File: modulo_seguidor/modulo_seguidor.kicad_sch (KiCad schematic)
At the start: 28 parts, among them J1 Battery, J2 Motor A Entradas, J4 Motor IZQ Arduino OUTPUT, J6 puerto sensores, M1 Motor_IZQ, M2 Motor_DER, SW1 SW_Push, SW2 SW_Nidec_CAS-120A1, U1 LM7806_TO220, U2 L298N

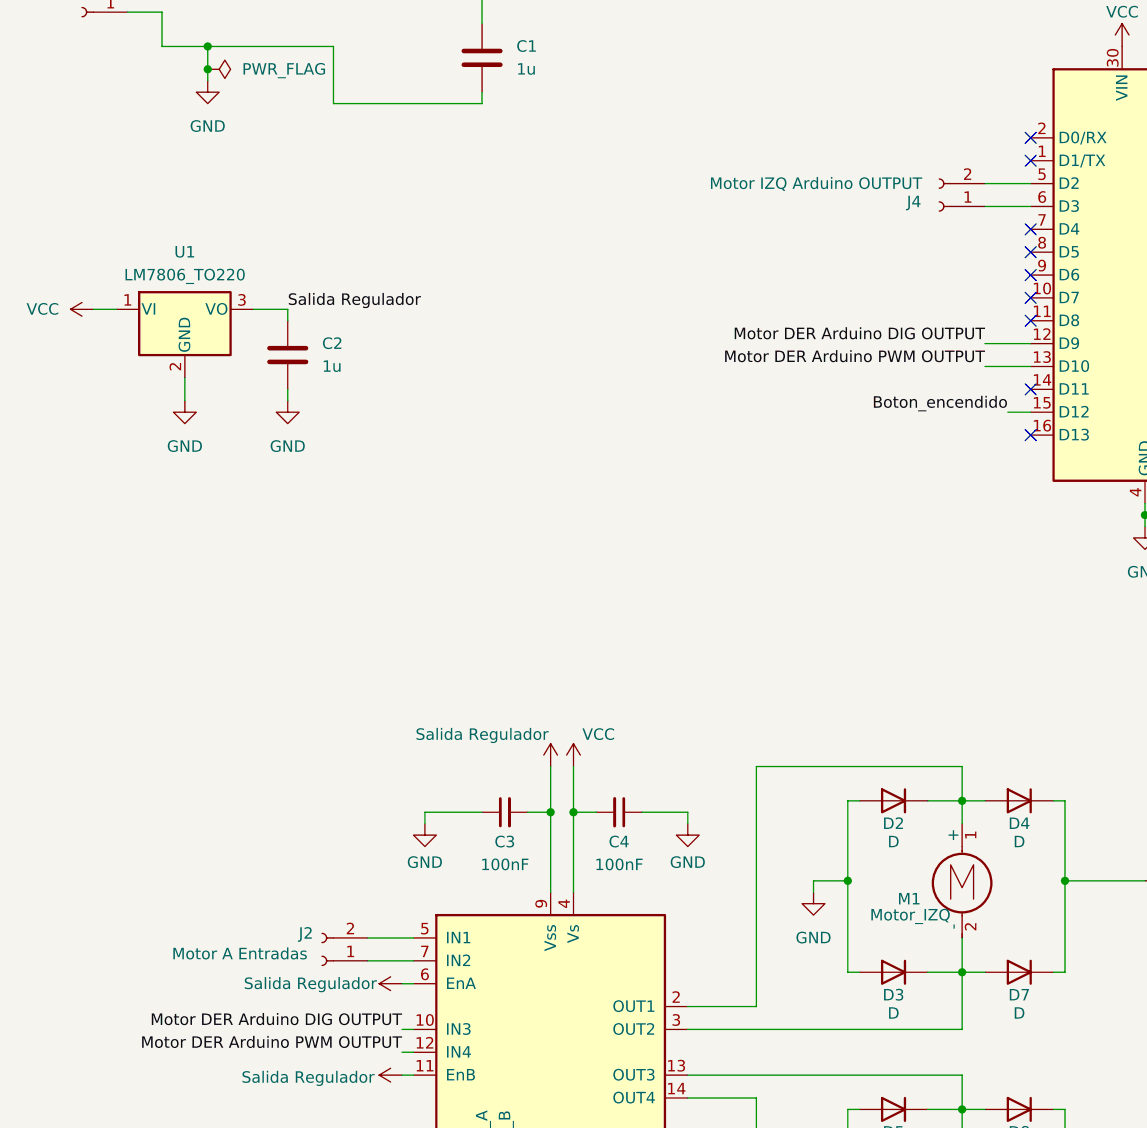
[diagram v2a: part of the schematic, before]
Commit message: refactor(modulo-seguidor): Elimino jumpers por cables soldados
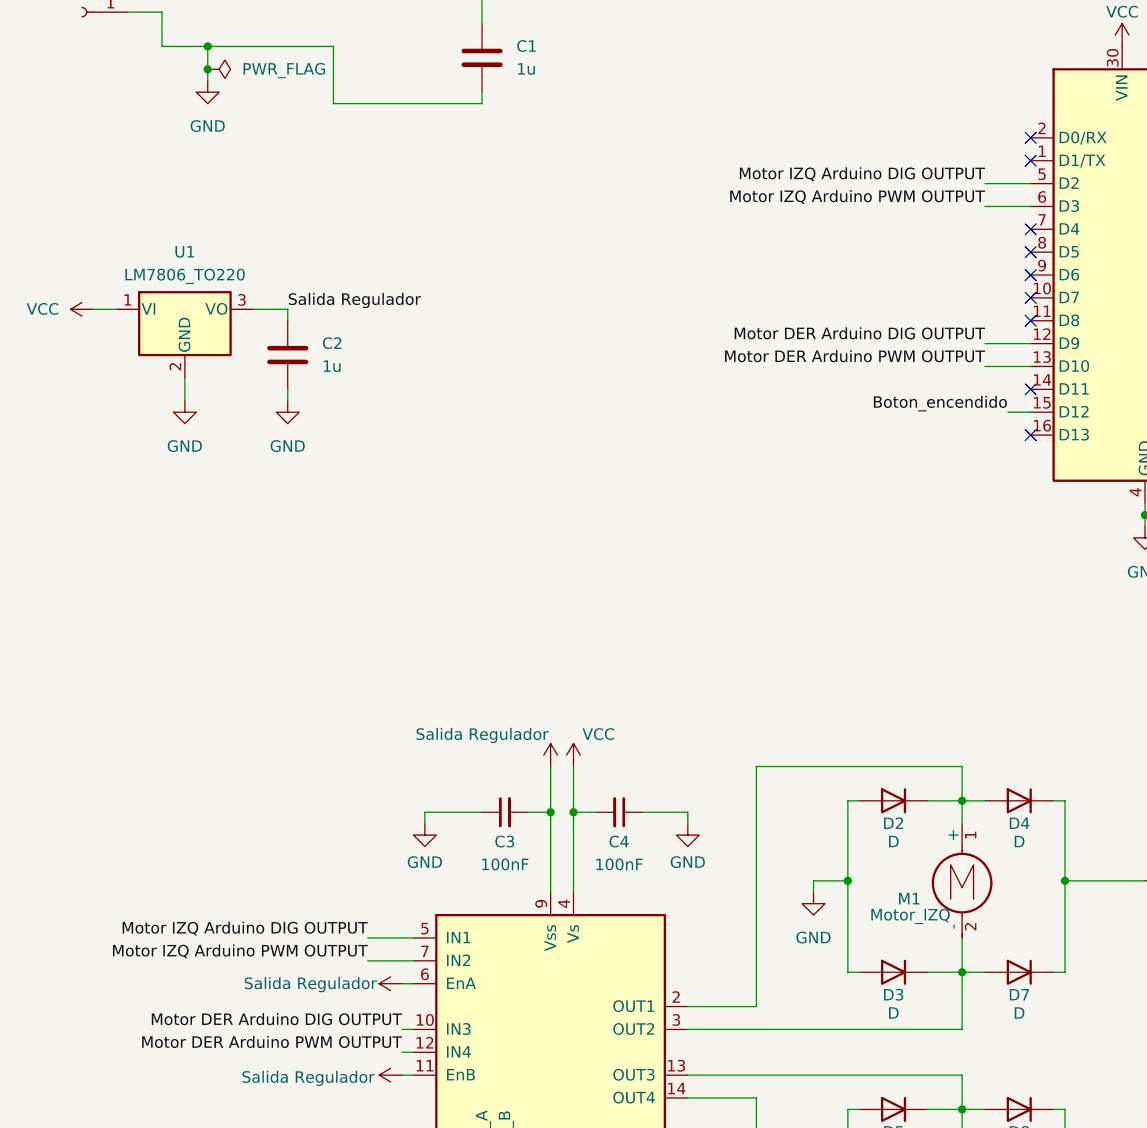
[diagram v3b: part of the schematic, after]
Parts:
- removed J2: Motor A Entradas, Connector_Molex:Molex_KK-254_AE-6410-02A_1x02_P2.54mm_Vertical, symbol Connector:Conn_01x02_Socket
- removed J4: Motor IZQ Arduino OUTPUT, Connector_Molex:Molex_KK-254_AE-6410-02A_1x02_P2.54mm_Vertical, symbol Connector:Conn_01x02_Socket
- J6: footprint Connector_PinHeader_2.54mm:PinHeader_1x08_P2.54mm_Horizontal -> Connector_PinHeader_2.54mm:PinHeader_1x08_P2.54mm_Vertical
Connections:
- net Motor IZQ Arduino PWM OUTPUT: now reaches U2.7 (IN2)
- net Motor IZQ Arduino PWM OUTPUT: now also A1.6 (D3)
- net Motor IZQ Arduino DIG OUTPUT: now reaches U2.5 (IN1)
- net Motor IZQ Arduino DIG OUTPUT: now also A1.5 (D2)
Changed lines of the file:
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@@
+		)
+	)
+	(label "Motor IZQ Arduino PWM OUTPUT"
+		(at 59.69 138.43 180)
+		(effects
+			(font
+				(size 1.27 1.27)
+			)
+			(justify right bottom)
 		)
 	)
@@
 		)
 	)
+	(label "Motor IZQ Arduino DIG OUTPUT"
+		(at 59.69 135.89 180)
+		(effects
+			(font
+				(size 1.27 1.27)
+			)
+			(justify right bottom)
+		)
+	)
 	(label "Sensor2"
 		(at 237.49 34.29 180)
@@
 		)
 	)
+	(label "Motor IZQ Arduino PWM OUTPUT"
+		(at 128.27 54.61 180)
+		(effects
+			(font
+				(size 1.27 1.27)
+			)
+			(justify right bottom)
+		)
+	)
 	(label "Sensor5"
 		(at 237.49 41.91 180)
@@
 		)
 	)
-	(symbol
-		(lib_id "Connector:Conn_01x02_Socket")
-		(at 54.61 138.43 180)
-		(unit 1)
-		(exclude_from_sim no)
-		(in_bom yes)
-		(on_board yes)
-		(dnp no)
-		(property "Reference" "J2"
-			(at 52.832 135.382 0)
-			(effects
-				(font
-					(size 1.27 1.27)
-				)
-			)
-		)
-		(property "Value" "Motor A Entradas"
-			(at 45.466 137.668 0)
-			(effects
-				(font
-					(size 1.27 1.27)
-				)
-			)
-		)
-		(property "Footprint" "Connector_Molex:Molex_KK-254_AE-6410-02A_1x02_P2.54mm_Vertical"
-			(at 54.61 138.43 0)
-			(effects
-				(font
-					(size 1.27 1.27)
-				)
-				(hide yes)
-			)
-		)
-		(property "Datasheet" "~"
-			(at 54.61 138.43 0)
-			(effects
-				(font
-					(size 1.27 1.27)
-				)
-				(hide yes)
-			)
-		)
-		(property "Description" "Generic connector, single row, 01x02, script generated"
-			(at 54.61 138.43 0)
-			(effects
-				(font
-					(size 1.27 1.27)
-				)
-				(hide yes)
-			)
-		)
-		(pin "1"
-		)
-		(pin "2"
-		)
-		(instances
-			(project "modulo_seguidor"
-				(path "/506ff443-80b5-4c22-9098-af8632a73945"
-					(reference "J2")
-					(unit 1)
-				)
-			)
+	(label "Motor IZQ Arduino DIG OUTPUT"
+		(at 128.27 52.07 180)
+		(effects
+			(font
+				(size 1.27 1.27)
+			)
+			(justify right bottom)
 		)
 	)
@@
 	)
 	(symbol
-		(lib_id "Connector:Conn_01x02_Socket")
-		(at 123.19 54.61 180)
-		(unit 1)
-		(exclude_from_sim no)
-		(in_bom yes)
-		(on_board yes)
-		(dnp no)
-		(property "Reference" "J4"
-			(at 120.396 54.102 0)
-			(effects
-				(font
-					(size 1.27 1.27)
-				)
-			)
-		)
-		(property "Value" "Motor IZQ Arduino OUTPUT"
-			(at 109.474 52.07 0)
-			(effects
-				(font
-					(size 1.27 1.27)
-				)
-			)
-		)
-		(property "Footprint" "Connector_Molex:Molex_KK-254_AE-6410-02A_1x02_P2.54mm_Vertical"
-			(at 123.19 54.61 0)
-			(effects
-				(font
-					(size 1.27 1.27)
-				)
-				(hide yes)
-			)
-		)
-		(property "Datasheet" "~"
-			(at 123.19 54.61 0)
-			(effects
-				(font
-					(size 1.27 1.27)
-				)
-				(hide yes)
-			)
-		)
-		(property "Description" "Generic connector, single row, 01x02, script generated"
-			(at 123.19 54.61 0)
-			(effects
-				(font
-					(size 1.27 1.27)
-				)
-				(hide yes)
-			)
-		)
-		(pin "1"
-		)
-		(pin "2"
-		)
-		(instances
-			(project "modulo_seguidor"
-				(path "/506ff443-80b5-4c22-9098-af8632a73945"
-					(reference "J4")
-					(unit 1)
-				)
-			)
-		)
-	)
-	(symbol
 		(lib_id "power:+5V")
 		(at 151.13 36.83 0)
@@
 			)
 		)
-		(property "Footprint" "Connector_PinHeader_2.54mm:PinHeader_1x08_P2.54mm_Horizontal"
+		(property "Footprint" "Connector_PinHeader_2.54mm:PinHeader_1x08_P2.54mm_Vertical"
 			(at 246.38 39.37 0)
 			(effects
